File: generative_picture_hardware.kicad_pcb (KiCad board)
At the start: 2 copper layers, 100 x 100 mm, 73 parts, among them J1 e_Paper_HAT, J2 Conn_ARM_JTAG_SWD_10, J3 USB_C_Receptacle_USB2.0, Q1 PMN48XP, Q2 DMG9926UDM, Q3 MBT3904DW1, SW1 SW_Push, SW2 SW_Push, U1 AP2112K-3.3, U2 ESP32-WROOM-32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

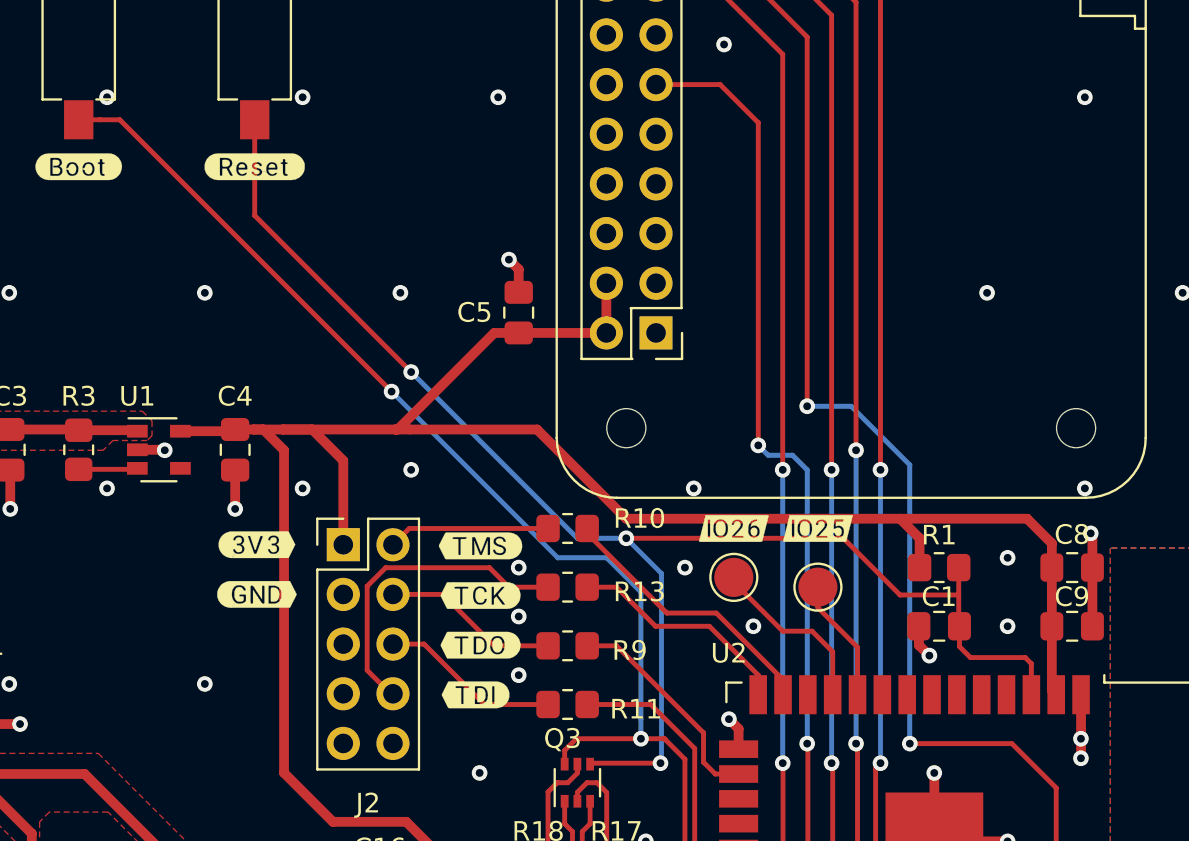
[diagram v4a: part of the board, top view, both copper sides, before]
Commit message: Uses copper fills for 3v3 rail
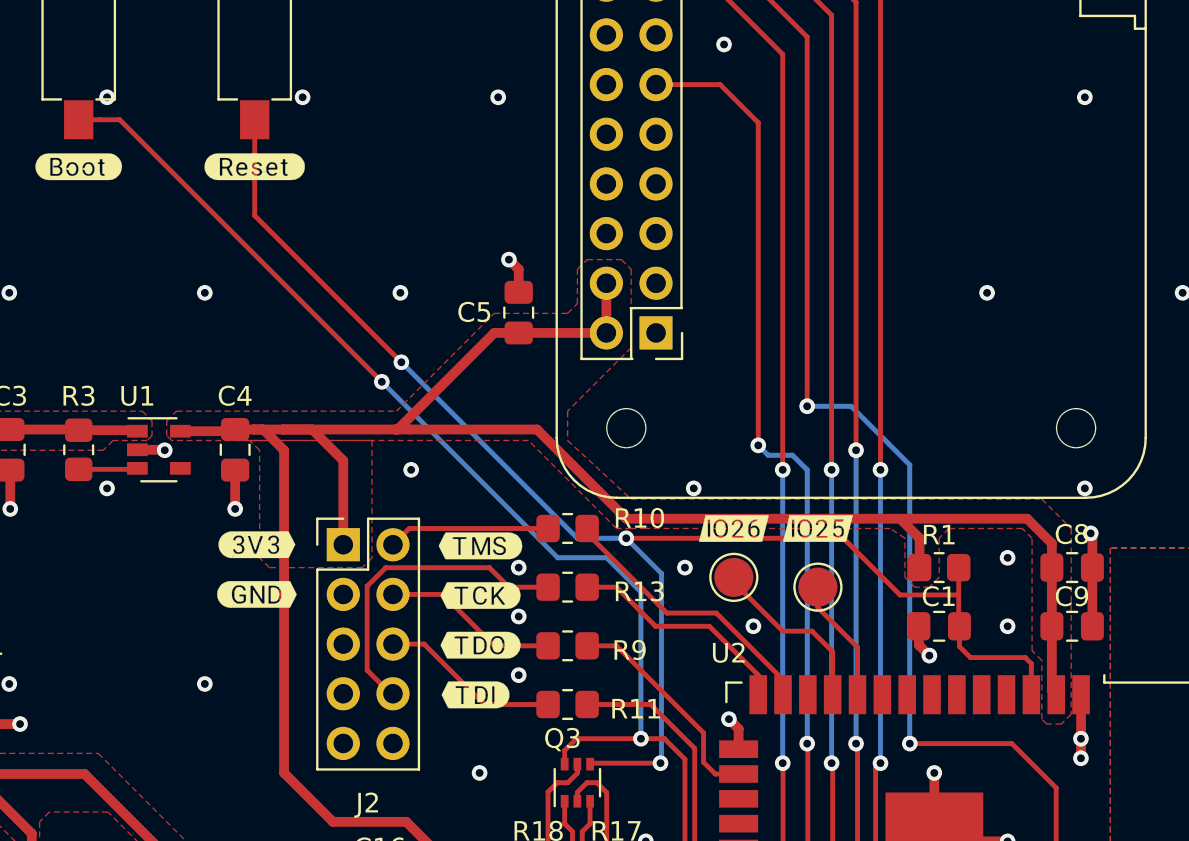
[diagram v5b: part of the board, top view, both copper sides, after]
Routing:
- net GND: vias 112 -> 111
- added copper zone on F.Cu, net +3V3
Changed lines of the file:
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@@
   (via (at 174.25 128.75) (size 0.8) (drill 0.4) (layers "F.Cu" "B.Cu") (net 3))
   (via (at 187.449748 66.949748) (size 0.8) (drill 0.4) (layers "F.Cu" "B.Cu") (free) (net 3))
-  (via (at 152.449748 116.949748) (size 0.8) (drill 0.4) (layers "F.Cu" "B.Cu") (free) (net 3))
   (via (at 192.25 141.25) (size 0.8) (drill 0.4) (layers "F.Cu" "B.Cu") (net 3))
   (via (at 137.449748 66.949748) (size 0.8) (drill 0.4) (layers "F.Cu" "B.Cu") (free) (net 3))
@@
   (segment (start 186 122.4) (end 186 123.9625) (width 0.25) (layer "F.Cu") (net 4))
   (segment (start 167.2 131) (end 167.15 131.05) (width 0.25) (layer "F.Cu") (net 4))
-  (segment (start 150 98.1) (end 150 103) (width 0.25) (layer "F.Cu") (net 4))
   (segment (start 189.715 125.915) (end 189.715 127.499748) (width 0.25) (layer "F.Cu") (net 4))
+  (segment (start 157.5 110.5) (end 150 103) (width 0.25) (layer "F.Cu") (net 4))
   (segment (start 183 122.4) (end 186 122.4) (width 0.25) (layer "F.Cu") (net 4))
   (segment (start 180.1 119.5) (end 183 122.4) (width 0.25) (layer "F.Cu") (net 4))
@@
   (segment (start 186.0375 125.0375) (end 186.6 125.6) (width 0.25) (layer "F.Cu") (net 4))
   (segment (start 186.6 125.6) (end 189.4 125.6) (width 0.25) (layer "F.Cu") (net 4))
+  (segment (start 150 103) (end 150 98.1) (width 0.25) (layer "F.Cu") (net 4))
   (segment (start 186.0375 124) (end 186.0375 125.0375) (width 0.25) (layer "F.Cu") (net 4))
   (segment (start 169 119.5) (end 180.1 119.5) (width 0.25) (layer "F.Cu") (net 4))
   (segment (start 170.75 131) (end 167.2 131) (width 0.25) (layer "F.Cu") (net 4))
   (segment (start 189.4 125.6) (end 189.715 125.915) (width 0.25) (layer "F.Cu") (net 4))
-  (segment (start 150 103) (end 158 111) (width 0.25) (layer "F.Cu") (net 4))
   (segment (start 186 123.9625) (end 186.0375 124) (width 0.25) (layer "F.Cu") (net 4))
+  (via (at 157.5 110.5) (size 0.8) (drill 0.4) (layers "F.Cu" "B.Cu") (net 4))
   (via (at 170.75 131) (size 0.8) (drill 0.4) (layers "F.Cu" "B.Cu") (net 4))
   (via (at 169 119.5) (size 0.8) (drill 0.4) (layers "F.Cu" "B.Cu") (net 4))
-  (via (at 158 111) (size 0.8) (drill 0.4) (layers "F.Cu" "B.Cu") (net 4))
-  (segment (start 166.5 119.5) (end 158 111) (width 0.25) (layer "B.Cu") (net 4))
+  (segment (start 157.5 110.5) (end 166.5 119.5) (width 0.25) (layer "B.Cu") (net 4))
+  (segment (start 166.5 119.5) (end 169 119.5) (width 0.25) (layer "B.Cu") (net 4))
   (segment (start 170.8 121.3) (end 170.8 130.95) (width 0.25) (layer "B.Cu") (net 4))
-  (segment (start 169 119.5) (end 166.5 119.5) (width 0.25) (layer "B.Cu") (net 4))
   (segment (start 170.8 130.95) (end 170.75 131) (width 0.25) (layer "B.Cu") (net 4))
   (segment (start 169 119.5) (end 170.8 121.3) (width 0.25) (layer "B.Cu") (net 4))
-  (segment (start 157 112) (end 143.1 98.1) (width 0.25) (layer "F.Cu") (net 5))
   (segment (start 170.95 129.75) (end 171 129.8) (width 0.25) (layer "F.Cu") (net 5))
+  (segment (start 156.5 111.5) (end 143.1 98.1) (width 0.25) (layer "F.Cu") (net 5))
+  (segment (start 142.1 98.1) (end 141 98.1) (width 0.25) (layer "F.Cu") (net 5))
   (segment (start 143.1 98.1) (end 142.1 98.1) (width 0.25) (layer "F.Cu") (net 5))
   (segment (start 170.95 129.75) (end 172 130.8) (width 0.25) (layer "F.Cu") (net 5))
@@
   (segment (start 172 144.2125) (end 172.0375 144.25) (width 0.25) (layer "F.Cu") (net 5))
   (segment (start 165.85 130.35) (end 166.45 129.75) (width 0.25) (layer "F.Cu") (net 5))
-  (segment (start 142.1 98.1) (end 141 98.1) (width 0.25) (layer "F.Cu") (net 5))
   (segment (start 172 130.8) (end 172 141) (width 0.25) (layer "F.Cu") (net 5))
   (segment (start 166.45 129.75) (end 169.75 129.75) (width 0.25) (layer "F.Cu") (net 5))
   (segment (start 172 141) (end 172 144.2125) (width 0.25) (layer "F.Cu") (net 5))
-  (via (at 157 112) (size 0.8) (drill 0.4) (layers "F.Cu" "B.Cu") (net 5))
+  (via (at 156.5 111.5) (size 0.8) (drill 0.4) (layers "F.Cu" "B.Cu") (net 5))
   (via (at 169.75 129.75) (size 0.8) (drill 0.4) (layers "F.Cu" "B.Cu") (net 5))
-  (segment (start 168 120.5) (end 165.5 120.5) (width 0.25) (layer "B.Cu") (net 5))
-  (segment (start 169.75 128.75) (end 169.75 122.25) (width 0.25) (layer "B.Cu") (net 5))
-  (segment (start 165.5 120.5) (end 157 112) (width 0.25) (layer "B.Cu") (net 5))
+  (segment (start 169.75 122.25) (end 169.75 128.75) (width 0.25) (layer "B.Cu") (net 5))
   (segment (start 169.75 128.75) (end 169.75 129.75) (width 0.25) (layer "B.Cu") (net 5))
-  (segment (start 169.75 122.25) (end 168 120.5) (width 0.25) (layer "B.Cu") (net 5))
+  (segment (start 156.5 111.5) (end 165.5 120.5) (width 0.25) (layer "B.Cu") (net 5))
+  (segment (start 168 120.5) (end 169.75 122.25) (width 0.25) (layer "B.Cu") (net 5))
+  (segment (start 165.5 120.5) (end 168 120.5) (width 0.25) (layer "B.Cu") (net 5))
   (segment (start 136.0625 113.9375) (end 133.7625 116.2375) (width 0.5) (layer "F.Cu") (net 6))
   (segment (start 141 113.975) (end 143.95 113.975) (width 0.5) (layer "F.Cu") (net 6))
@@
     )
   )
+  (zone (net 7) (net_name "+3V3") (layer "F.Cu") (hatch edge 0.508)
+    (priority 1)
+    (connect_pads (clearance 0.508))
+    (min_thickness 0.254) (filled_areas_thickness no)
+    (fill yes (thermal_gap 0.508) (thermal_bridge_width 0.508))
+    (polygon
+      (pts
+        (xy 156 120.5)
+        (xy 155.5 121)
+        (xy 150.75 121)
+        (xy 150.25 120.5)
+        (xy 150.25 115)
+        (xy 149.75 114.5)
+        (xy 156 114.5)
+      )
+    )
+  )
   (zone (net 6) (net_name "VCC") (layer "F.Cu") (hatch edge 0.508)
     (priority 1)
@@
       )
     )
+  )
+  (zone (net 7) (net_name "+3V3") (layer "F.Cu") (hatch edge 0.508)
+    (priority 1)
+    (connect_pads (clearance 0.508))
+    (min_thickness 0.254) (filled_areas_thickness no)
+    (fill yes (thermal_gap 0.508) (thermal_bridge_width 0.508))
+    (polygon
+      (pts
+        (xy 169.25 105.75)
+        (xy 169.25 109.75)
+        (xy 166 113)
+        (xy 166 114.5)
+        (xy 169.25 117.5)
+        (xy 190.25 117.5)
+        (xy 191.75 119)
+        (xy 191.75 128.5)
+        (xy 191.25 129)
+        (xy 190.5 129)
+        (xy 190.25 128.75)
+        (xy 190.25 125.75)
+        (xy 189.75 125.25)
+        (xy 189.75 119.5)
+        (xy 189.25 119)
+        (xy 185.5 119)
+        (xy 185 119.5)
+        (xy 185 121.5)
+        (xy 184.5 122)
+        (xy 183.75 122)
+        (xy 183.25 121.5)
+        (xy 183.25 119.5)
+        (xy 182.5 119)
+        (xy 170 119)
+        (xy 169.25 119)
+        (xy 168.5 119)
+        (xy 164 114.5)
+        (xy 145.75 114.5)
+        (xy 145.5 114.25)
+        (xy 145.5 113.5)
+        (xy 146 113)
+        (xy 157.25 113)
+        (xy 162.25 108)
+        (xy 166 108)
+        (xy 166.5 107.5)
+        (xy 166.5 105.75)
+        (xy 167 105.25)
+        (xy 168.75 105.25)
+      )
+    )

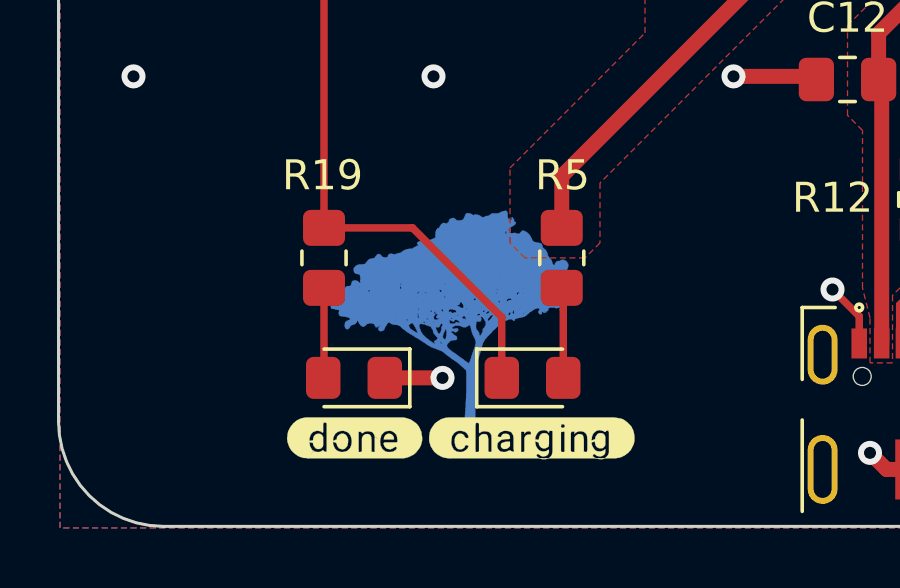
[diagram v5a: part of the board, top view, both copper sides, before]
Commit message: Adjust logo position
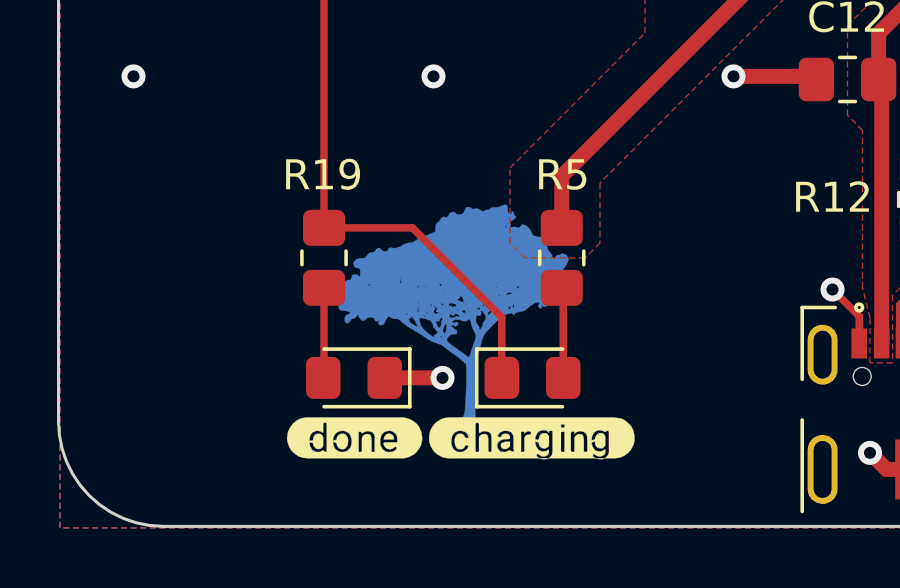
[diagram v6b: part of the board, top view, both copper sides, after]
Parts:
- moved Ref** 0.20 mm to (113.0, 149.8)
- moved Ref** 0.20 mm to (113.0, 144.8)
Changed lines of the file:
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@@
   )
   (footprint "Amieiro:url_bsilks" (layer "F.Cu")
-    (at 112.988912 150)
+    (at 112.988912 149.8)
     (attr through_hole)
     (fp_text reference "Ref**" (at 0 0) (layer "F.SilkS") hide
@@
   )
   (footprint "Amieiro:ipe_logo" (layer "F.Cu")
-    (at 113 145)
+    (at 113 144.8)
     (attr through_hole)
     (fp_text reference "Ref**" (at 0 0) (layer "F.SilkS") hide
